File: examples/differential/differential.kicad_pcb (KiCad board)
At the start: 2 copper layers, 4 x 16 mm, 8 parts

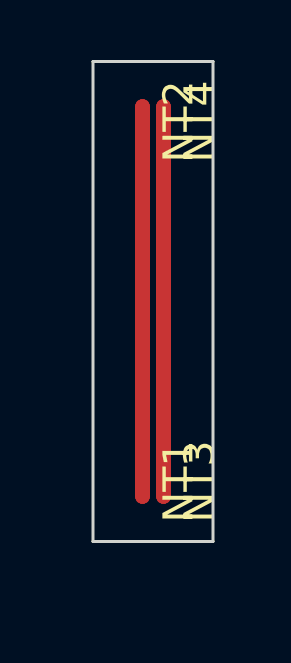
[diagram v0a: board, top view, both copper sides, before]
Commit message: Update examples with corrected settings and keep track of exported gerbers
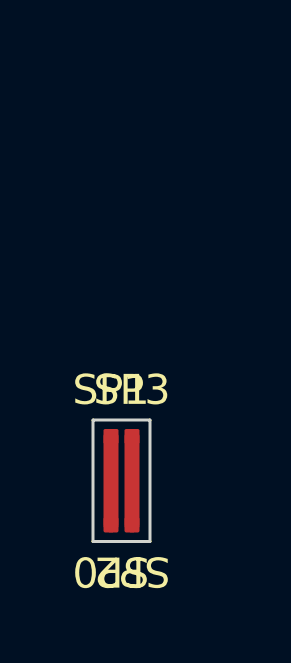
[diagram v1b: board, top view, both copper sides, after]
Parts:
- removed NT1, NT2, NT3, NT4: NetTie_2, NetTie:NetTie-2_SMD_Pad0.5mm
- SP0, SP1, SP2, SP3: footprint antmicro-footprints:Simulation_Port -> simulation_port:pad_0.5mm
- moved SP1 14.2 mm to (148.6, 128.4), turned to 0 degrees
- moved SP3 14.2 mm to (149.3, 128.4), turned to 0 degrees
- moved SP0 2.48 mm to (148.6, 125.5), turned to 180 degrees
- moved SP2 2.48 mm to (149.3, 125.5), turned to 180 degrees
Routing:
- net /A_-: track 11.0 -> 2.95 mm
- net /A_+: track 11.0 -> 2.95 mm
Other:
- board size 4 x 16 mm -> 1.9 x 4 mm
